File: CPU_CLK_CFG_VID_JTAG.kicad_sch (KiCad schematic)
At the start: 1 part

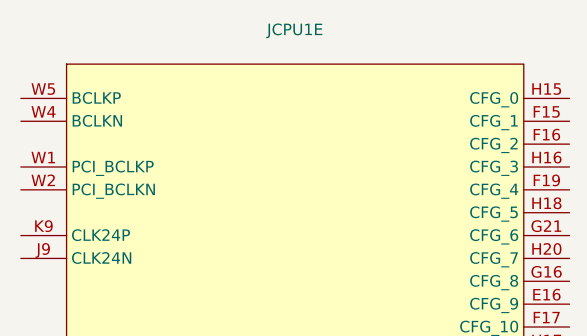
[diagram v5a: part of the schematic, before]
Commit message: Added first PCH symbol and footprint
THANKS @mothenjoyer69 so much for extracting and converting the PCH footprint from a laptop boardview ❤️
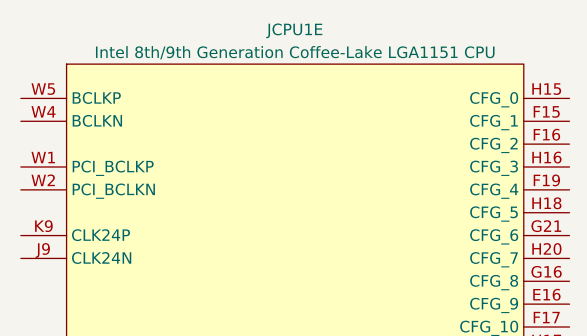
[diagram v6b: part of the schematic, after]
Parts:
- JCPU1: value ~ -> Intel 8th/9th Generation Coffee-Lake LGA1151 CPU

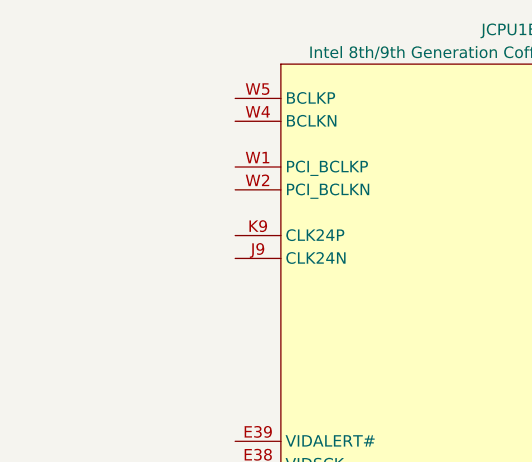
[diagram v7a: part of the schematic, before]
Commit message: Added pcie slot and cpu clocks
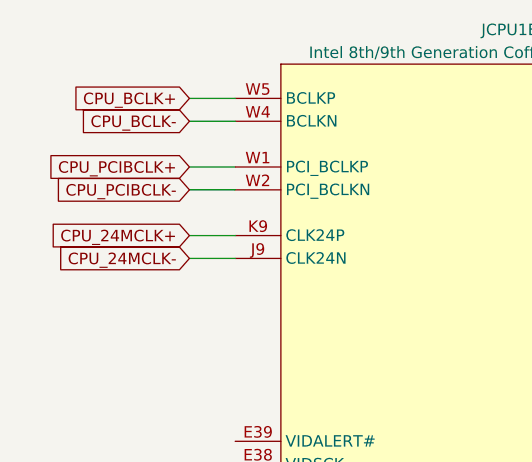
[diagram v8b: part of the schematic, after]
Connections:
- net CPU_24MCLK-: now reaches JCPU1.J9 (CLK24N)
- net CPU_24MCLK+: now reaches JCPU1.K9 (CLK24P)
- net CPU_PCIBCLK+: now reaches JCPU1.W1 (PCI_BCLKP)
- net CPU_PCIBCLK-: now reaches JCPU1.W2 (PCI_BCLKN)
- net CPU_BCLK-: now reaches JCPU1.W4 (BCLKN)
- net CPU_BCLK+: now reaches JCPU1.W5 (BCLKP)
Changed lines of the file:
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@@
 		(company "WifiCable")
+	)
+	(wire
+		(pts
+			(xy 106.68 46.99) (xy 111.76 46.99)
+		)
+		(stroke
+			(width 0)
+			(type default)
+		)
+	)
+	(wire
+		(pts
+			(xy 106.68 62.23) (xy 111.76 62.23)
+		)
+		(stroke
+			(width 0)
+			(type default)
+		)
+	)
+	(wire
+		(pts
+			(xy 106.68 59.69) (xy 111.76 59.69)
+		)
+		(stroke
+			(width 0)
+			(type default)
+		)
+	)
+	(wire
+		(pts
+			(xy 106.68 44.45) (xy 111.76 44.45)
+		)
+		(stroke
+			(width 0)
+			(type default)
+		)
+	)
+	(wire
+		(pts
+			(xy 106.68 54.61) (xy 111.76 54.61)
+		)
+		(stroke
+			(width 0)
+			(type default)
+		)
+	)
+	(wire
+		(pts
+			(xy 106.68 52.07) (xy 111.76 52.07)
+		)
+		(stroke
+			(width 0)
+			(type default)
+		)
+	)
+	(global_label "CPU_24MCLK-"
+		(shape input)
+		(at 106.68 62.23 180)
+		(fields_autoplaced yes)
+		(effects
+			(font
+				(size 1.27 1.27)
+			)
+			(justify right)
+		)
+		(property "Intersheetrefs" "${INTERSHEET_REFS}"
+			(at 86.2171 62.23 0)
+			(effects
+				(font
+					(size 1.27 1.27)
+				)
+				(justify right)
+				(hide yes)
+			)
+		)
+	)
+	(global_label "CPU_PCIBCLK-"
+		(shape input)
+		(at 106.68 54.61 180)
+		(fields_autoplaced yes)
+		(effects
+			(font
+				(size 1.27 1.27)
+			)
+			(justify right)
+		)
+		(property "Intersheetrefs" "${INTERSHEET_REFS}"
+			(at 86.2171 54.61 0)
+			(effects
+				(font
+					(size 1.27 1.27)
+				)
+				(justify right)
+				(hide yes)
+			)
+		)
+	)
+	(global_label "CPU_BCLK+"
+		(shape input)
+		(at 106.68 44.45 180)
+		(fields_autoplaced yes)
+		(effects
+			(font
+				(size 1.27 1.27)
+			)
+			(justify right)
+		)
+		(property "Intersheetrefs" "${INTERSHEET_REFS}"
+			(at 86.2171 44.45 0)
+			(effects
+				(font
+					(size 1.27 1.27)
+				)
+				(justify right)
+				(hide yes)
+			)
+		)
+	)
+	(global_label "CPU_PCIBCLK+"
+		(shape input)
+		(at 106.68 52.07 180)
+		(fields_autoplaced yes)
+		(effects
+			(font
+				(size 1.27 1.27)
+			)
+			(justify right)
+		)
+		(property "Intersheetrefs" "${INTERSHEET_REFS}"
+			(at 86.2171 52.07 0)
+			(effects
+				(font
+					(size 1.27 1.27)
+				)
+				(justify right)
+				(hide yes)
+			)
+		)
+	)
+	(global_label "CPU_BCLK-"
+		(shape input)
+		(at 106.68 46.99 180)
+		(fields_autoplaced yes)
+		(effects
+			(font
+				(size 1.27 1.27)
+			)
+			(justify right)
+		)
+		(property "Intersheetrefs" "${INTERSHEET_REFS}"
+			(at 86.2171 46.99 0)
+			(effects
+				(font
+					(size 1.27 1.27)
+				)
+				(justify right)
+				(hide yes)
+			)
+		)
+	)
+	(global_label "CPU_24MCLK+"
+		(shape input)
+		(at 106.68 59.69 180)
+		(fields_autoplaced yes)
+		(effects
+			(font
+				(size 1.27 1.27)
+			)
+			(justify right)
+		)
+		(property "Intersheetrefs" "${INTERSHEET_REFS}"
+			(at 86.2171 59.69 0)
+			(effects
+				(font
+					(size 1.27 1.27)
+				)
+				(justify right)
+				(hide yes)
+			)
+		)
 	)
 	(symbol
